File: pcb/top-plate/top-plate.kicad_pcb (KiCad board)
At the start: 2 copper layers, 285.8 x 116.7 mm, 87 parts

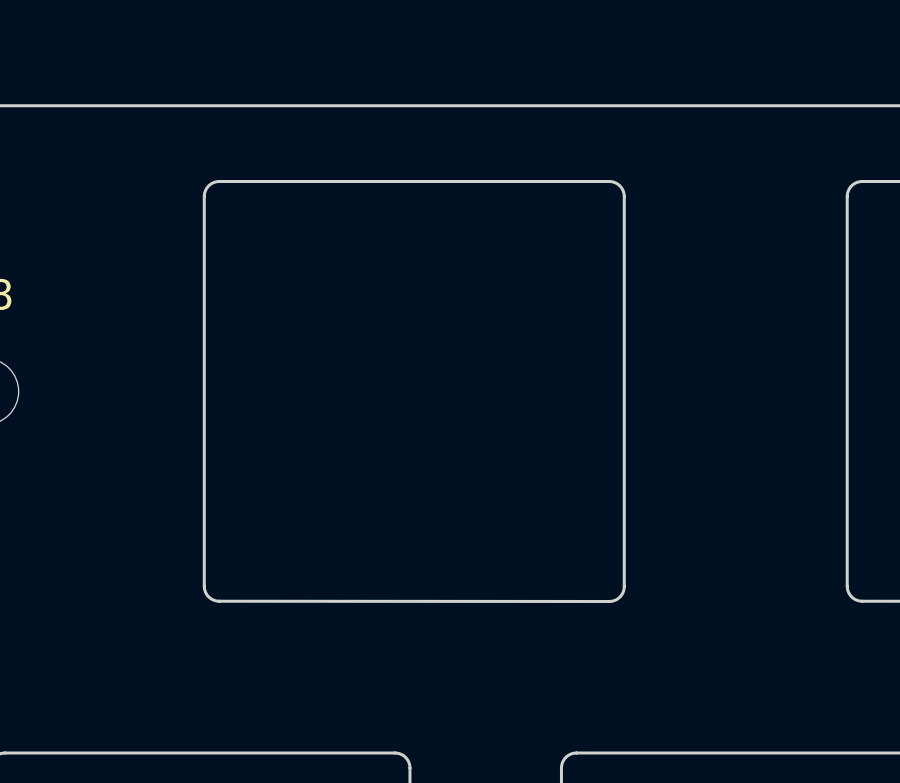
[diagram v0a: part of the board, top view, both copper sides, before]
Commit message: Move the top plate F5 key to the proper spot
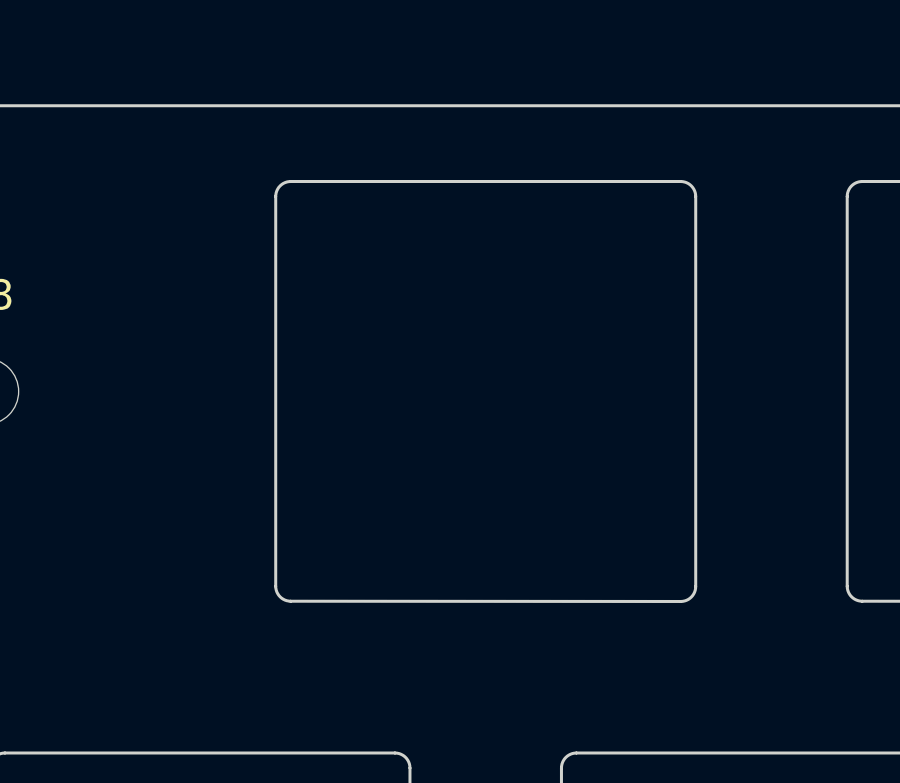
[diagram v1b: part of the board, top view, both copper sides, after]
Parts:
- moved REF** 2.38 mm to (152.4, 31.0)
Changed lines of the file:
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@@
     (fp_line (start -6.5 7) (end 6.499672 7.000007) (layer "Edge.Cuts") (width 0.1))
     (fp_arc (start 53 -6) (mid 53.353553 -5.853553) (end 53.5 -5.5) (layer "Edge.Cuts") (width 0.1))
-    (fp_arc (start 6.999672 5.500007) (mid 7.146107 5.146441) (end 7.499672 5.000007) (layer "Edge.Cuts") (width 0.1))
+    (fp_arc (start 6.999672 5.500007) (mid 7.146108 5.146445) (end 7.499672 5.000007) (layer "Edge.Cuts") (width 0.1))
     (fp_arc (start 47.975 6.5) (mid 48.328553 6.646447) (end 48.475 7) (layer "Edge.Cuts") (width 0.1))
     (fp_arc (start 46.25 5) (mid 46.603553 5.146447) (end 46.75 5.5) (layer "Edge.Cuts") (width 0.1))
@@
     (fp_arc (start -53 6.5) (mid -53.353553 6.353553) (end -53.5 6) (layer "Edge.Cuts") (width 0.1))
     (fp_arc (start -7 -5.5) (mid -7.146447 -5.146447) (end -7.5 -5) (layer "Edge.Cuts") (width 0.1))
-    (fp_arc (start 6.999672 6.500007) (mid 6.853214 6.853548) (end 6.499672 7.000007) (layer "Edge.Cuts") (width 0.1))
+    (fp_arc (start 6.999672 6.500007) (mid 6.853215 6.853551) (end 6.499672 7.000007) (layer "Edge.Cuts") (width 0.1))
     (fp_arc (start 51.775 7) (mid 51.921447 6.646447) (end 52.275 6.5) (layer "Edge.Cuts") (width 0.1))
     (fp_arc (start -53.5 -5.5) (mid -53.353553 -5.853553) (end -53 -6) (layer "Edge.Cuts") (width 0.1))
@@
   )
   (footprint "bschwind_slots:mx_top_plate_1.00u" (layer "F.Cu")
-    (at 150.01875 30.95625)
-    (attr through_hole)
-    (fp_text reference "REF**" (at 0 2.38125) (layer "Eco1.User")
+    (at 152.4 30.95625)
+    (attr through_hole)
+    (fp_text reference "REF**" (at 0 2.38125) (layer "Eco1.User")

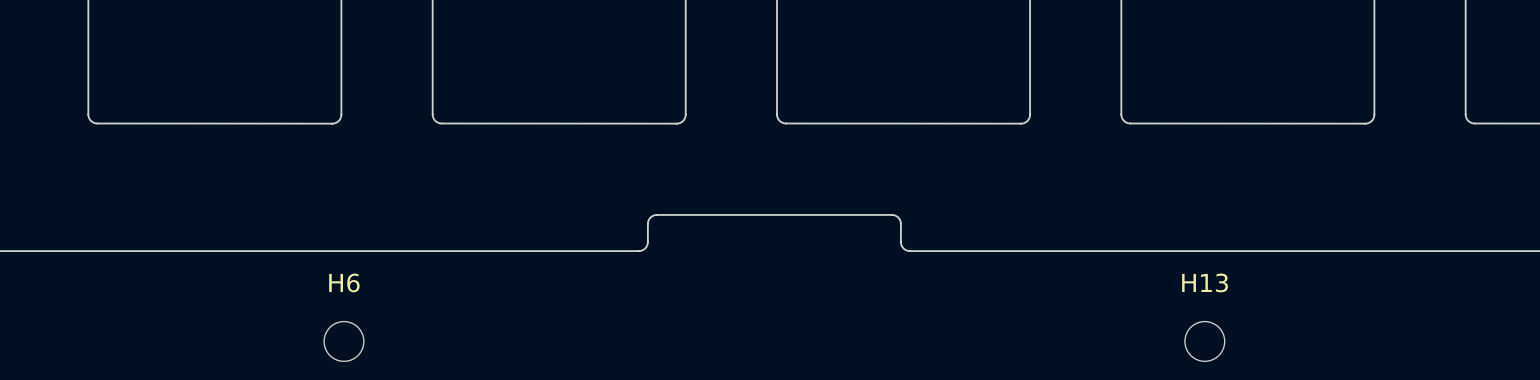
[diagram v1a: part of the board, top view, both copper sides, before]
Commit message: Adjust the silkscreen to be on the front side, mark it v0.2
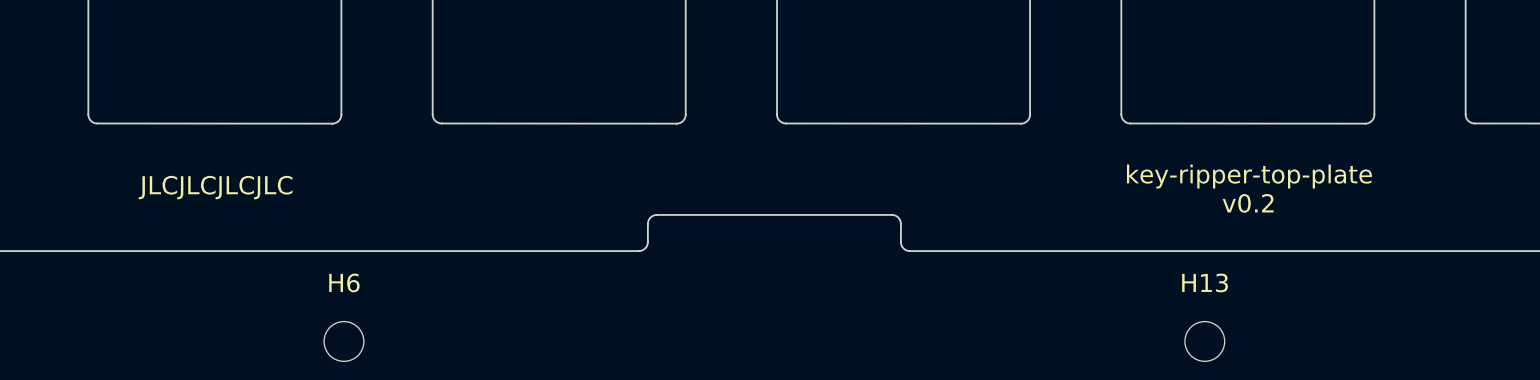
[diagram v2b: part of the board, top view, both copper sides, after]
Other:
- board text added: "key-ripper-top-plate v0.2"
- board text removed: "key-ripper-top-plate v0.1"
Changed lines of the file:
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@@
     (pad_to_mask_clearance 0)
     (pcbplotparams
-      (layerselection 0x00010fc_ffffffff)
+      (layerselection 0x00010fc_7fffffff)
       (disableapertmacros false)
-      (usegerberextensions false)
-      (usegerberattributes true)
-      (usegerberadvancedattributes true)
-      (creategerberjobfile true)
+      (usegerberextensions true)
+      (usegerberattributes false)
+      (usegerberadvancedattributes false)
+      (creategerberjobfile false)
       (svguseinch false)
       (svgprecision 6)
@@
       (psa4output false)
       (plotreference true)
-      (plotvalue true)
+      (plotvalue false)
       (plotinvisibletext false)
       (sketchpadsonfab false)
-      (subtractmaskfromsilk false)
+      (subtractmaskfromsilk true)
       (outputformat 1)
       (mirror false)
-      (drillshape 1)
+      (drillshape 0)
       (scaleselection 1)
-      (outputdirectory "")
+      (outputdirectory "production/gerber/v0.2/")
     )
   )
@@
     (fp_line (start -6.5 7) (end 6.499672 7.000007) (layer "Edge.Cuts") (width 0.1))
     (fp_arc (start 53 -6) (mid 53.353553 -5.853553) (end 53.5 -5.5) (layer "Edge.Cuts") (width 0.1))
-    (fp_arc (start 6.999672 5.500007) (mid 7.146108 5.146445) (end 7.499672 5.000007) (layer "Edge.Cuts") (width 0.1))
+    (fp_arc (start 6.999672 5.500007) (mid 7.146107 5.146441) (end 7.499672 5.000007) (layer "Edge.Cuts") (width 0.1))
     (fp_arc (start 47.975 6.5) (mid 48.328553 6.646447) (end 48.475 7) (layer "Edge.Cuts") (width 0.1))
     (fp_arc (start 46.25 5) (mid 46.603553 5.146447) (end 46.75 5.5) (layer "Edge.Cuts") (width 0.1))
@@
     (fp_arc (start -53 6.5) (mid -53.353553 6.353553) (end -53.5 6) (layer "Edge.Cuts") (width 0.1))
     (fp_arc (start -7 -5.5) (mid -7.146447 -5.146447) (end -7.5 -5) (layer "Edge.Cuts") (width 0.1))
-    (fp_arc (start 6.999672 6.500007) (mid 6.853215 6.853551) (end 6.499672 7.000007) (layer "Edge.Cuts") (width 0.1))
+    (fp_arc (start 6.999672 6.500007) (mid 6.853214 6.853548) (end 6.499672 7.000007) (layer "Edge.Cuts") (width 0.1))
     (fp_arc (start 51.775 7) (mid 51.921447 6.646447) (end 52.275 6.5) (layer "Edge.Cuts") (width 0.1))
     (fp_arc (start -53.5 -5.5) (mid -53.353553 -5.853553) (end -53 -6) (layer "Edge.Cuts") (width 0.1))
@@
   (gr_line (start 304.8 23.8125) (end 304.8 133.35) (layer "Edge.Cuts") (width 0.1))
   (gr_arc (start 304.8 133.35) (mid 304.102533 135.033783) (end 302.41875 135.73125) (layer "Edge.Cuts") (width 0.1))
-  (gr_text "key-ripper-top-plate\nv0.1" (at 295.275 107.15625) (layer "B.SilkS")
-    (effects (font (size 1 1) (thickness 0.15)) (justify mirror))
-  )
-  (gr_text "JLCJLCJLCJLC" (at 295.6 115.3) (layer "B.SilkS")
-    (effects (font (size 1 1) (thickness 0.15)) (justify mirror))
+  (gr_text "key-ripper-top-plate\nv0.2" (at 185.8 117.8) (layer "F.SilkS")
+    (effects (font (size 1 1) (thickness 0.15)))
+  )
+  (gr_text "JLCJLCJLCJLC" (at 128.7 117.6) (layer "F.SilkS")
+    (effects (font (size 1 1) (thickness 0.15)))
   )
   (zone (net 0) (net_name "") (layer "F.Cu") (hatch edge 0.508)

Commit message: Clean up the top-plate
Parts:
- removed H10, H11, H12, H13, H14, H15, H16, H5, H6, H7, H8, H9: M_HOLE, MountingHole:MountingHole_2.2mm_M2
- moved REF** 2.38 mm to (123.8, 31.0)
- moved REF** 2.38 mm to (104.8, 31.0)
- moved REF** 2.38 mm to (66.7, 31.0)
- moved REF** 2.38 mm to (85.7, 31.0)
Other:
- board size 285.8 x 116.7 mm -> 285.8 x 114.3 mm
- board text added: "key-ripper-top-plate v0.3"
- board text removed: "key-ripper-top-plate v0.2"

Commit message: Re-align top plate to the same grid as the PCB
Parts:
- moved REF** 2.38 mm to (95.2, 66.7)
- moved REF** 2.38 mm to (223.8, 104.8)
- moved REF** 2.38 mm to (147.6, 104.8)
- moved REF** 2.38 mm to (233.4, 85.7)
- moved REF** 2.38 mm to (176.2, 85.7)
- moved REF** 2.38 mm to (152.4, 66.7)
- moved REF** 2.38 mm to (283.4, 85.7)
- moved REF** 2.38 mm to (157.2, 85.7)
- moved REF** 2.38 mm to (33.3, 66.7)
- moved REF** 2.38 mm to (133.3, 66.7)
- moved REF** 2.38 mm to (90.5, 104.8)
- moved REF** 2.38 mm to (119.1, 85.7)
- moved REF** 2.38 mm to (35.7, 85.7)
- moved REF** 2.38 mm to (190.5, 66.7)
- moved REF** 2.38 mm to (252.4, 85.7)
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
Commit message: Add M2 holes in the top plate
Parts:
- added REF**: MountingHole_2.2mm_M2, MountingHole:MountingHole_2.2mm_M2, F.Cu at (138.1, 21.6)
- added REF**: MountingHole_2.2mm_M2, MountingHole:MountingHole_2.2mm_M2, F.Cu at (100.0, 130.8)
- added REF**: MountingHole_2.2mm_M2, MountingHole:MountingHole_2.2mm_M2, F.Cu at (302.3, 76.2)
- added REF**: MountingHole_2.2mm_M2, MountingHole:MountingHole_2.2mm_M2, F.Cu at (223.8, 21.6)
- added REF**: MountingHole_2.2mm_M2, MountingHole:MountingHole_2.2mm_M2, F.Cu at (219.1, 130.8)
- added REF**: MountingHole_2.2mm_M2, MountingHole:MountingHole_2.2mm_M2, F.Cu at (21.6, 76.2)
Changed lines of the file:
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@@
     (fp_arc (start 6.5 -7) (mid 6.853553 -6.853553) (end 7 -6.5) (layer "Edge.Cuts") (width 0.1))
+  )
+  (footprint "MountingHole:MountingHole_2.2mm_M2" (layer "F.Cu")
+    (at 21.55 76.2)
+    (descr "Mounting Hole 2.2mm, no annular, M2")
+    (tags "mounting hole 2.2mm no annular m2")
+    (attr exclude_from_pos_files exclude_from_bom)
+    (fp_text reference "REF**" (at 0 -3.2) (layer "F.SilkS")
+      (effects (font (size 1 1) (thickness 0.15)))
+    )
+    (fp_text value "MountingHole_2.2mm_M2" (at 0 3.2) (layer "F.Fab")
+      (effects (font (size 1 1) (thickness 0.15)))
+    )
+    (fp_text user "${REFERENCE}" (at 0 0) (layer "F.Fab")
+      (effects (font (size 1 1) (thickness 0.15)))
+    )
+    (fp_circle (center 0 0) (end 2.2 0) (layer "Cmts.User") (width 0.15) (fill none))
+    (fp_circle (center 0 0) (end 2.45 0) (layer "F.CrtYd") (width 0.05) (fill none))
+    (pad "" np_thru_hole circle (at 0 0) (size 2.2 2.2) (drill 2.2) (layers *.Cu *.Mask))
   )
   (footprint "bschwind_slots:mx_top_plate_1.00u" (layer "F.Cu")
@@
     (fp_arc (start 6.5 -7) (mid 6.853553 -6.853553) (end 7 -6.5) (layer "Edge.Cuts") (width 0.1))
     (fp_arc (start -6.5 6.990924) (mid -6.853553 6.844477) (end -7 6.490924) (layer "Edge.Cuts") (width 0.1))
+  )
+  (footprint "MountingHole:MountingHole_2.2mm_M2" (layer "F.Cu")
+    (at 138.125 21.55)
+    (descr "Mounting Hole 2.2mm, no annular, M2")
+    (tags "mounting hole 2.2mm no annular m2")
+    (attr exclude_from_pos_files exclude_from_bom)
+    (fp_text reference "REF**" (at 0 -3.2) (layer "F.SilkS")
+      (effects (font (size 1 1) (thickness 0.15)))
+    )
+    (fp_text value "MountingHole_2.2mm_M2" (at 0 3.2) (layer "F.Fab")
+      (effects (font (size 1 1) (thickness 0.15)))
+    )
+    (fp_text user "${REFERENCE}" (at 0 0) (layer "F.Fab")
+      (effects (font (size 1 1) (thickness 0.15)))
+    )
+    (fp_circle (center 0 0) (end 2.2 0) (layer "Cmts.User") (width 0.15) (fill none))
+    (fp_circle (center 0 0) (end 2.45 0) (layer "F.CrtYd") (width 0.05) (fill none))
+    (pad "" np_thru_hole circle (at 0 0) (size 2.2 2.2) (drill 2.2) (layers *.Cu *.Mask))
   )
   (footprint "bschwind_slots:mx_top_plate_1.00u" (layer "F.Cu")
@@
     (fp_arc (start -7 -6.5) (mid -6.853553 -6.853553) (end -6.5 -7) (layer "Edge.Cuts") (width 0.1))
   )
+  (footprint "MountingHole:MountingHole_2.2mm_M2" (layer "F.Cu")
+    (at 100 130.85)
+    (descr "Mounting Hole 2.2mm, no annular, M2")
+    (tags "mounting hole 2.2mm no annular m2")
+    (attr exclude_from_pos_files exclude_from_bom)
+    (fp_text reference "REF**" (at 0 -3.2) (layer "F.SilkS")
+      (effects (font (size 1 1) (thickness 0.15)))
+    )
+    (fp_text value "MountingHole_2.2mm_M2" (at 0 3.2) (layer "F.Fab")
+      (effects (font (size 1 1) (thickness 0.15)))
+    )
+    (fp_text user "${REFERENCE}" (at 0 0) (layer "F.Fab")
+      (effects (font (size 1 1) (thickness 0.15)))
+    )
+    (fp_circle (center 0 0) (end 2.2 0) (layer "Cmts.User") (width 0.15) (fill none))
+    (fp_circle (center 0 0) (end 2.45 0) (layer "F.CrtYd") (width 0.05) (fill none))
+    (pad "" np_thru_hole circle (at 0 0) (size 2.2 2.2) (drill 2.2) (layers *.Cu *.Mask))
+  )
   (footprint "bschwind_slots:mx_top_plate_1.00u" (layer "F.Cu")
     (at 133.35 66.67505)
@@
     (fp_arc (start 7 6.5) (mid 6.853553 6.853553) (end 6.5 7) (layer "Edge.Cuts") (width 0.1))
     (fp_arc (start -7 -6.5) (mid -6.853553 -6.853553) (end -6.5 -7) (layer "Edge.Cuts") (width 0.1))
+  )
+  (footprint "MountingHole:MountingHole_2.2mm_M2" (layer "F.Cu")
+    (at 302.3 76.2)
+    (descr "Mounting Hole 2.2mm, no annular, M2")
+    (tags "mounting hole 2.2mm no annular m2")
+    (attr exclude_from_pos_files exclude_from_bom)
+    (fp_text reference "REF**" (at 0 -3.2) (layer "F.SilkS")
+      (effects (font (size 1 1) (thickness 0.15)))
+    )
+    (fp_text value "MountingHole_2.2mm_M2" (at 0 3.2) (layer "F.Fab")
+      (effects (font (size 1 1) (thickness 0.15)))
+    )
+    (fp_text user "${REFERENCE}" (at 0 0) (layer "F.Fab")
+      (effects (font (size 1 1) (thickness 0.15)))
+    )
+    (fp_circle (center 0 0) (end 2.2 0) (layer "Cmts.User") (width 0.15) (fill none))
+    (fp_circle (center 0 0) (end 2.45 0) (layer "F.CrtYd") (width 0.05) (fill none))
+    (pad "" np_thru_hole circle (at 0 0) (size 2.2 2.2) (drill 2.2) (layers *.Cu *.Mask))
   )
   (footprint "bschwind_slots:mx_top_plate_1.25u" (layer "F.Cu")
@@
     (fp_arc (start -7 -6.5) (mid -6.853553 -6.853553) (end -6.5 -7) (layer "Edge.Cuts") (width 0.1))
   )
-  (footprint "bschwind_slots:mx_top_plate_1.00u" (layer "F.Cu")
+  (footprint "MountingHole:MountingHole_2.2mm_M2" (layer "F.Cu")
+    (at 223.8 21.55)
+    (descr "Mounting Hole 2.2mm, no annular, M2")
+    (tags "mounting hole 2.2mm no annular m2")
+    (attr exclude_from_pos_files exclude_from_bom)
+    (fp_text reference "REF**" (at 0 -3.2) (layer "F.SilkS")
+      (effects (font (size 1 1) (thickness 0.15)))
+    )
+    (fp_text value "MountingHole_2.2mm_M2" (at 0 3.2) (layer "F.Fab")
+      (effects (font (size 1 1) (thickness 0.15)))
+    )
+    (fp_text user "${REFERENCE}" (at 0 0) (layer "F.Fab")
+      (effects (font (size 1 1) (thickness 0.15)))
+    )
+    (fp_circle (center 0 0) (end 2.2 0) (layer "Cmts.User") (width 0.15) (fill none))
+    (fp_circle (center 0 0) (end 2.45 0) (layer "F.CrtYd") (width 0.05) (fill none))
+    (pad "" np_thru_hole circle (at 0 0) (size 2.2 2.2) (drill 2.2) (layers *.Cu *.Mask))
+  )
+  (footprint "MountingHole:MountingHole_2.2mm_M2" (layer "F.Cu")
+    (at 219.1 130.85)
+    (descr "Mounting Hole 2.2mm, no annular, M2")
+    (tags "mounting hole 2.2mm no annular m2")
+    (attr exclude_from_pos_files exclude_from_bom)
+    (fp_text reference "REF**" (at 0 -3.2) (layer "F.SilkS")
+      (effects (font (size 1 1) (thickness 0.15)))
+    )
+    (fp_text value "MountingHole_2.2mm_M2" (at 0 3.2) (layer "F.Fab")
+      (effects (font (size 1 1) (thickness 0.15)))
+    )
+    (fp_text user "${REFERENCE}" (at 0 0) (layer "F.Fab")
+      (effects (font (size 1 1) (thickness 0.15)))
+    )
+    (fp_circle (center 0 0) (end 2.2 0) (layer "Cmts.User") (width 0.15) (fill none))
+    (fp_circle (center 0 0) (end 2.45 0) (layer "F.CrtYd") (width 0.05) (fill none))
+    (pad "" np_thru_hole circle (at 0 0) (size 2.2 2.2) (drill 2.2) (layers *.Cu *.Mask))
+  )
+  (footprint "bschwind_slots:mx_top_plate_1.00u" (layer "F.Cu")
